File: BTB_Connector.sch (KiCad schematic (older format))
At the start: 1 part

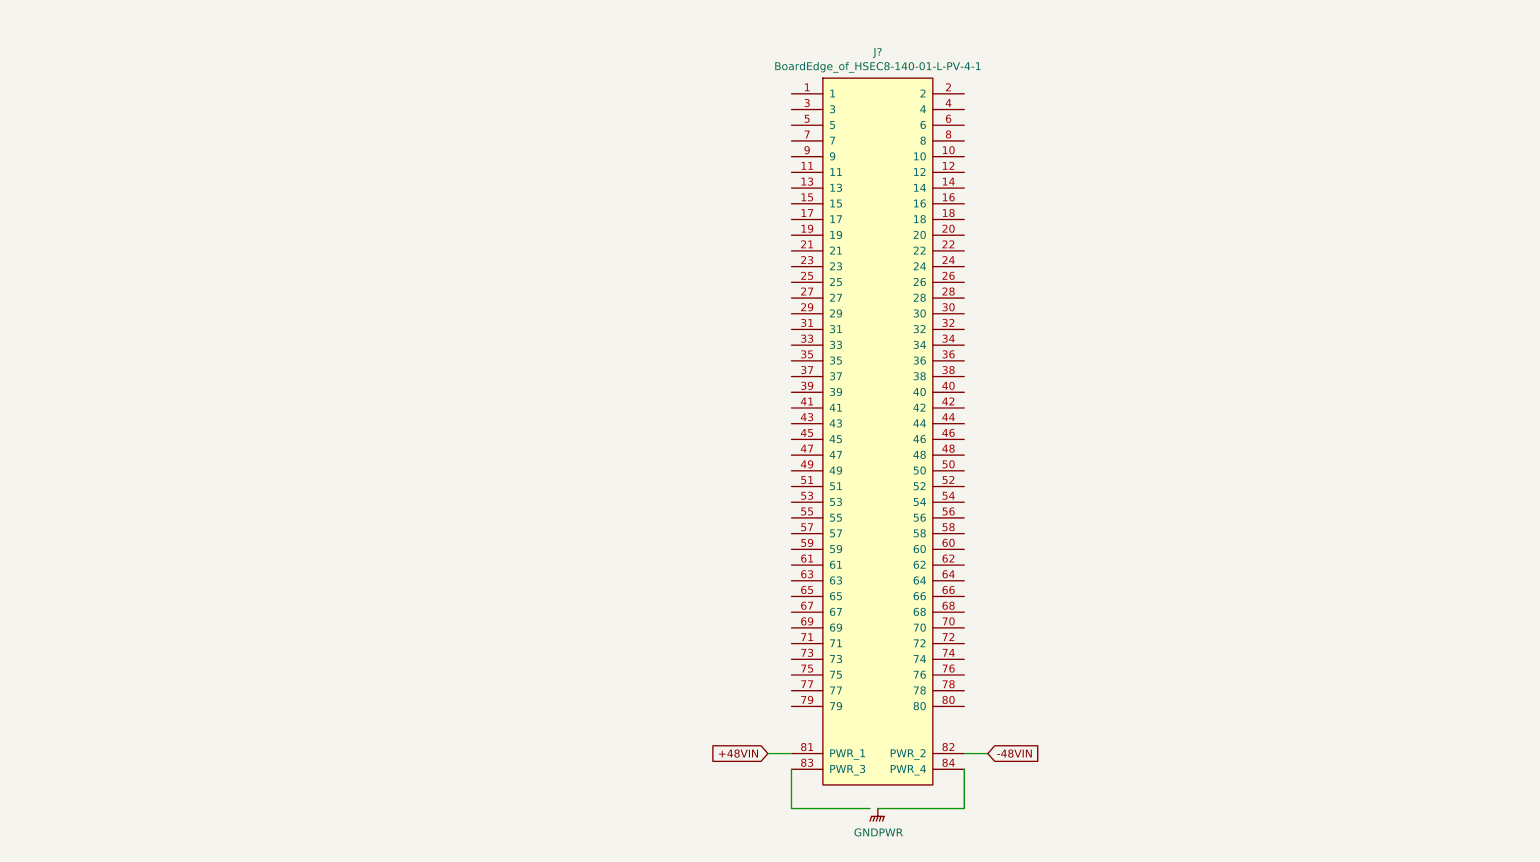
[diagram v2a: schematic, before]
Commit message: -Clock --GND pin was missing. it was added to pin 45 -BTB --pins added
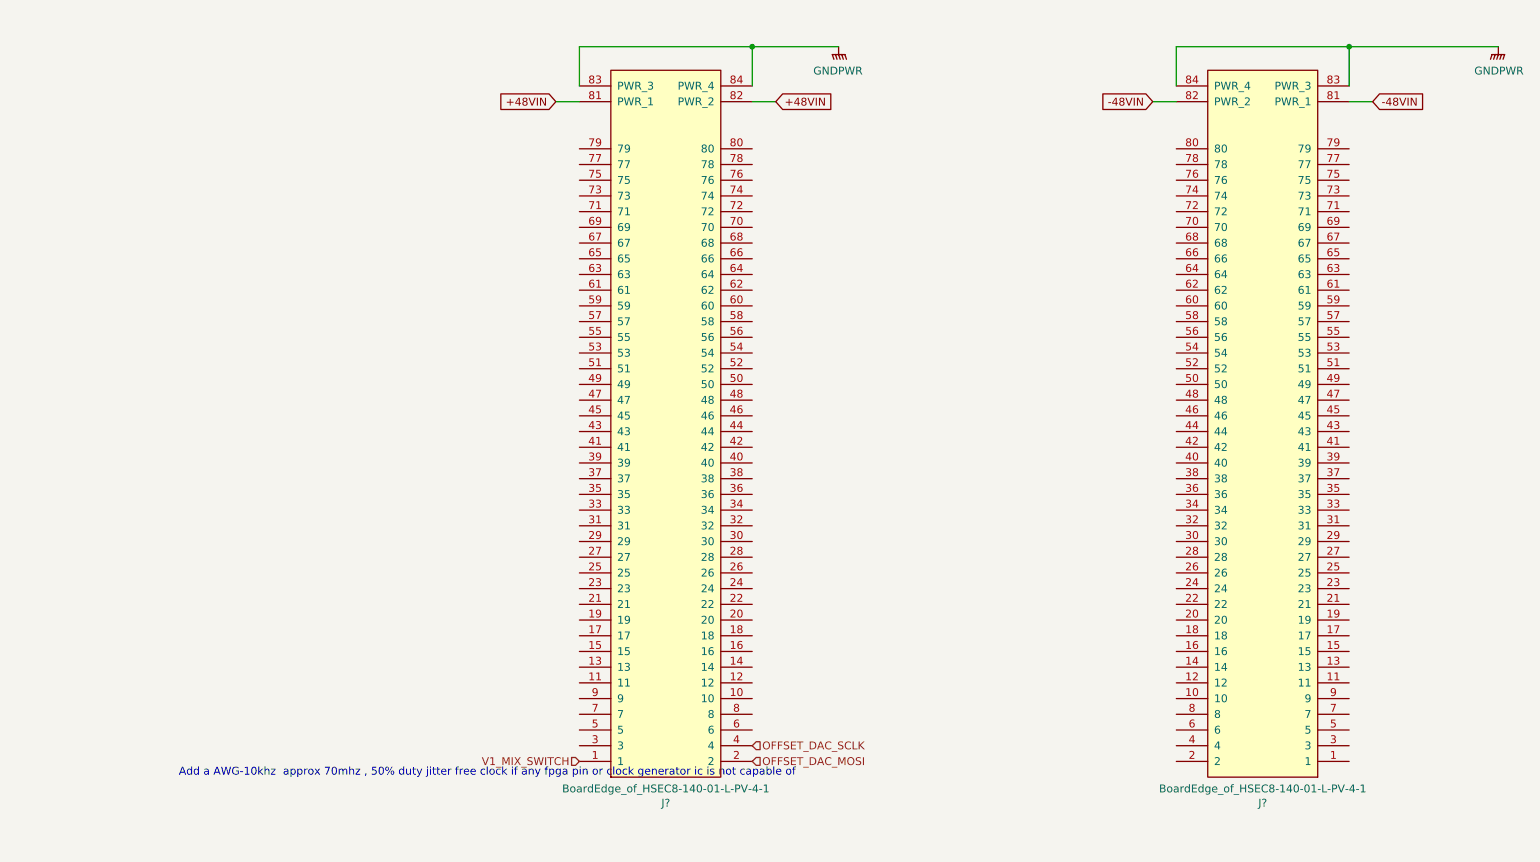
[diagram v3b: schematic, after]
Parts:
- added J?: BoardEdge_of_HSEC8-140-01-L-PV-4-1, GM_Connectors:BoardEdge_of_HSEC8-140-01-L-PV-4-1, symbol GM_Connectors:BoardEdge_of_HSEC8-140-01-L-PV-4-1
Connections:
- net labels added: OFFSET_DAC_MOSI, OFFSET_DAC_SCLK, V1_MIX_SWITCH
- wire segments 6 -> 12
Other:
- note added: "Add a AWG-10khz approx 70mhz , 50% duty jitter free clock if any fpga pin or clock generator ic is not capable of"
- moved on the sheet: J?
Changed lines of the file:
@@
 Comment4 ""
 $EndDescr
+Text GLabel 3400 1650 0    50   Input ~ 0
++48VIN
+Text GLabel 4800 1650 2    50   Input ~ 0
++48VIN
+Wire Wire Line
+	4800 1650 4650 1650
+Wire Wire Line
+	3400 1650 3550 1650
+$Comp
+L power:GNDPWR #PWR?
+U 1 1 602FF0E5
+P 5200 1300
+AR Path="/60256C5F/602FF0E5" Ref="#PWR?"  Part="1"
+AR Path="/601E7B79/602FF0E5" Ref="#PWR?"  Part="1"
+F 0 "#PWR?" H 5200 1100 50  0001 C CNN
+F 1 "GNDPWR" H 5204 1146 50  0000 C CNN
+F 2 "" H 5200 1250 50  0001 C CNN
+F 3 "" H 5200 1250 50  0001 C CNN
+	1    5200 1300
+	-1   0    0    -1
+$EndComp
+Wire Wire Line
+	4650 1550 4650 1300
+Wire Wire Line
+	4650 1300 5200 1300
+Wire Wire Line
+	3550 1300 3550 1550
+$Comp
+L GM_Connectors:BoardEdge_of_HSEC8-140-01-L-PV-4-1 J?
+U 1 1 605943E0
+P 8250 5950
+F 0 "J?" H 8600 6115 50  0000 C CNN
+F 1 "BoardEdge_of_HSEC8-140-01-L-PV-4-1" H 8600 6024 50  0000 C CNN
+F 2 "GM_Connectors:BoardEdge_of_HSEC8-140-01-L-PV-4-1" H 8250 5950 50  0001 C CNN
+F 3 "http://suddendocs.samtec.com/prints/hsec8-1xx-xx-x-pv-x-x-xx-footprint.pdf" H 8250 5950 50  0001 C CNN
+	1    8250 5950
+	-1   0    0    1
+$EndComp
+Text GLabel 8600 1650 2    50   Input ~ 0
+-48VIN
+Text GLabel 7200 1650 0    50   Input ~ 0
+-48VIN
+Wire Wire Line
+	7200 1650 7350 1650
+Wire Wire Line
+	8600 1650 8450 1650
+$Comp
+L power:GNDPWR #PWR?
+U 1 1 6059456A
+P 9400 1300
+AR Path="/60256C5F/6059456A" Ref="#PWR?"  Part="1"
+AR Path="/601E7B79/6059456A" Ref="#PWR?"  Part="1"
+F 0 "#PWR?" H 9400 1100 50  0001 C CNN
+F 1 "GNDPWR" H 9404 1146 50  0000 C CNN
+F 2 "" H 9400 1250 50  0001 C CNN
+F 3 "" H 9400 1250 50  0001 C CNN
+	1    9400 1300
+	1    0    0    -1
+$EndComp
+Wire Wire Line
+	7350 1550 7350 1300
+Wire Wire Line
+	8450 1300 8450 1550
+Wire Wire Line
+	3550 1300 4650 1300
+Connection ~ 4650 1300
+Wire Wire Line
+	9400 1300 8450 1300
+Connection ~ 8450 1300
+Wire Wire Line
+	7350 1300 8450 1300
 $Comp
 L GM_Connectors:BoardEdge_of_HSEC8-140-01-L-PV-4-1 J?
 U 1 1 602EB3A8
-P 5100 1500
-F 0 "J?" H 5450 1665 50  0000 C CNN
-F 1 "BoardEdge_of_HSEC8-140-01-L-PV-4-1" H 5450 1574 50  0000 C CNN
-F 2 "GM_Connectors:BoardEdge_of_HSEC8-140-01-L-PV-4-1" H 5100 1500 50  0001 C CNN
-F 3 "http://suddendocs.samtec.com/prints/hsec8-1xx-xx-x-pv-x-x-xx-footprint.pdf" H 5100 1500 50  0001 C CNN
-	1    5100 1500
-	1    0    0    -1
+P 3750 5950
+F 0 "J?" H 4100 6115 50  0000 C CNN
+F 1 "BoardEdge_of_HSEC8-140-01-L-PV-4-1" H 4100 6024 50  0000 C CNN
+F 2 "GM_Connectors:BoardEdge_of_HSEC8-140-01-L-PV-4-1" H 3750 5950 50  0001 C CNN
+F 3 "http://suddendocs.samtec.com/prints/hsec8-1xx-xx-x-pv-x-x-xx-footprint.pdf" H 3750 5950 50  0001 C CNN
+	1    3750 5950
+	1    0    0    1
 $EndComp
-Text GLabel 4750 5800 0    50   Input ~ 0
-+48VIN
-Text GLabel 6150 5800 2    50   Input ~ 0
--48VIN
-Wire Wire Line
-	6150 5800 6000 5800
-Wire Wire Line
-	4750 5800 4900 5800
-$Comp
-L power:GNDPWR #PWR?
-U 1 1 602FF0E5
-P 5450 6150
-AR Path="/60256C5F/602FF0E5" Ref="#PWR?"  Part="1"
-AR Path="/601E7B79/602FF0E5" Ref="#PWR?"  Part="1"
-F 0 "#PWR?" H 5450 5950 50  0001 C CNN
-F 1 "GNDPWR" H 5454 5996 50  0000 C CNN
-F 2 "" H 5450 6100 50  0001 C CNN
-F 3 "" H 5450 6100 50  0001 C CNN
-	1    5450 6150
-	1    0    0    -1
-$EndComp
-Wire Wire Line
-	6000 5900 6000 6150
-Wire Wire Line
-	6000 6150 5450 6150
-Wire Wire Line
-	5400 6150 4900 6150
-Wire Wire Line
-	4900 6150 4900 5900
+Text HLabel 3550 5850 0    50   Input ~ 0
+V1_MIX_SWITCH
+Text HLabel 4650 5850 2    50   Input ~ 0
+OFFSET_DAC_MOSI
+Text HLabel 4650 5750 2    50   Input ~ 0
+OFFSET_DAC_SCLK
+Text Notes 1000 5950 0    50   ~ 0
+Add a AWG-10khz  approx 70mhz , 50% duty jitter free clock if any fpga pin or clock generator ic is not capable of
 $EndSCHEMATC

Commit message: PCB created and schematics annotated High speed connections added to the BTB
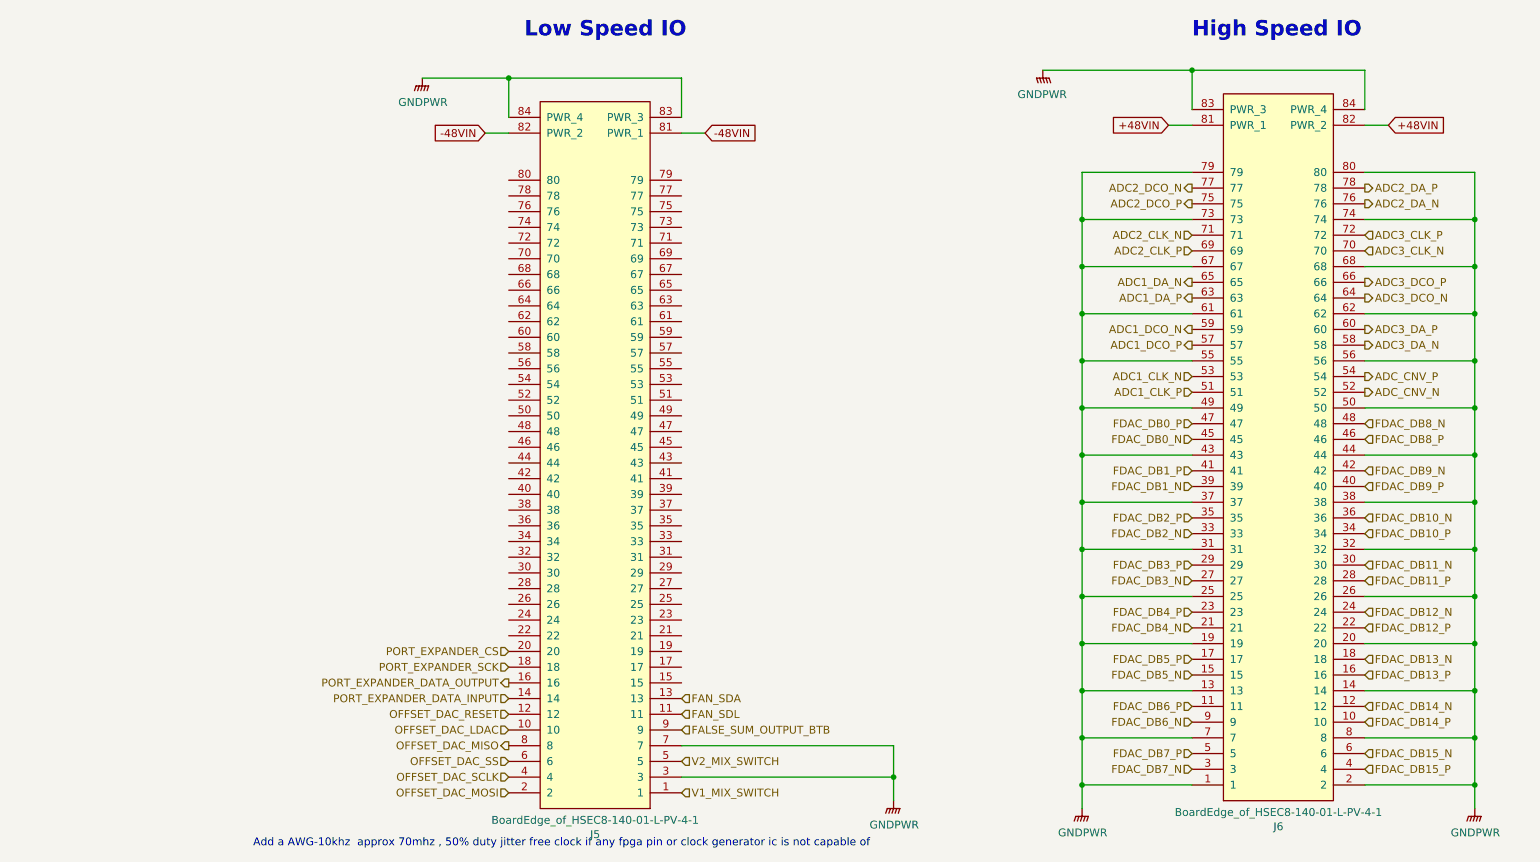
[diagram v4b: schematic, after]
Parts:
- J6: renamed from J?; footprint GM_Connectors:BoardEdge_of_HSEC8-140-01-L-PV-4-1 -> GM_Connectors:HSEC8-140-01-L-PV-4-1
- gave numbers to parts that had none: 1
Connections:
- net +48VIN: now also J6.81 (PWR_1), J6.82 (PWR_2); no longer J5.81 (PWR_1), J5.82 (PWR_2)
- net -48VIN: now also J5.81 (PWR_1), J5.82 (PWR_2); no longer J6.81 (PWR_1), J6.82 (PWR_2)
- net GNDPWR: now also J5.3, J5.7, J6.1, J6.13, J6.14, J6.19, J6.2, J6.20, J6.25, J6.26, J6.31, J6.32, J6.37, J6.38, J6.43, J6.44, J6.49, J6.50, J6.55, J6.56, J6.61, J6.62, J6.67, J6.68, J6.7, J6.73, J6.74, J6.79, J6.8, J6.80
- net OFFSET_DAC_LDAC: now reaches J5.10
- net FAN_SDL: now reaches J5.11
- net OFFSET_DAC_RESET: now reaches J5.12
- net FAN_SDA: now reaches J5.13
- net PORT_EXPANDER_DATA_INPUT: now reaches J5.14
- net PORT_EXPANDER_DATA_OUTPUT: now reaches J5.16
- net PORT_EXPANDER_SCK: now reaches J5.18
- net PORT_EXPANDER_CS: now reaches J5.20
- net V2_MIX_SWITCH: now reaches J5.5
- net OFFSET_DAC_SS: now reaches J5.6
- net OFFSET_DAC_MISO: now reaches J5.8
- net FALSE_SUM_OUTPUT_BTB: now reaches J5.9
- net FDAC_DB14_P: now reaches J6.10
- net FDAC_DB6_P: now reaches J6.11
- net FDAC_DB14_N: now reaches J6.12
- net FDAC_DB5_N: now reaches J6.15
- net FDAC_DB13_P: now reaches J6.16
- net FDAC_DB5_P: now reaches J6.17
- net FDAC_DB13_N: now reaches J6.18
- net FDAC_DB4_N: now reaches J6.21
- net FDAC_DB12_P: now reaches J6.22
- net FDAC_DB4_P: now reaches J6.23
- net FDAC_DB12_N: now reaches J6.24
- net FDAC_DB3_N: now reaches J6.27
- net FDAC_DB11_P: now reaches J6.28
- net FDAC_DB3_P: now reaches J6.29
- net FDAC_DB7_N: now reaches J6.3
- net FDAC_DB11_N: now reaches J6.30
- net FDAC_DB2_N: now reaches J6.33
- net FDAC_DB10_P: now reaches J6.34
- net FDAC_DB2_P: now reaches J6.35
- net FDAC_DB10_N: now reaches J6.36
- net FDAC_DB1_N: now reaches J6.39
- net FDAC_DB15_P: now reaches J6.4
- net FDAC_DB9_P: now reaches J6.40
- net FDAC_DB1_P: now reaches J6.41
- net FDAC_DB9_N: now reaches J6.42
- net FDAC_DB0_N: now reaches J6.45
- net FDAC_DB8_P: now reaches J6.46
- net FDAC_DB0_P: now reaches J6.47
- net FDAC_DB8_N: now reaches J6.48
- net FDAC_DB7_P: now reaches J6.5
- net ADC1_CLK_P: now reaches J6.51
- net ADC_CNV_N: now reaches J6.52
- net ADC1_CLK_N: now reaches J6.53
- net ADC_CNV_P: now reaches J6.54
- net ADC1_DCO_P: now reaches J6.57
- net ADC3_DA_N: now reaches J6.58
- net ADC1_DCO_N: now reaches J6.59
- net FDAC_DB15_N: now reaches J6.6
- net ADC3_DA_P: now reaches J6.60
- net ADC1_DA_P: now reaches J6.63
- net ADC3_DCO_N: now reaches J6.64
- net ADC1_DA_N: now reaches J6.65
- net ADC3_DCO_P: now reaches J6.66
- net ADC2_CLK_P: now reaches J6.69
- net ADC3_CLK_N: now reaches J6.70
- net ADC2_CLK_N: now reaches J6.71
- net ADC3_CLK_P: now reaches J6.72
- net ADC2_DCO_P: now reaches J6.75
- net ADC2_DA_N: now reaches J6.76
- net ADC2_DCO_N: now reaches J6.77
- net ADC2_DA_P: now reaches J6.78
- net FDAC_DB6_N: now reaches J6.9
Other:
- note added: "High Speed IO"
- note added: "Low Speed IO"
- moved on the sheet: J5, J6

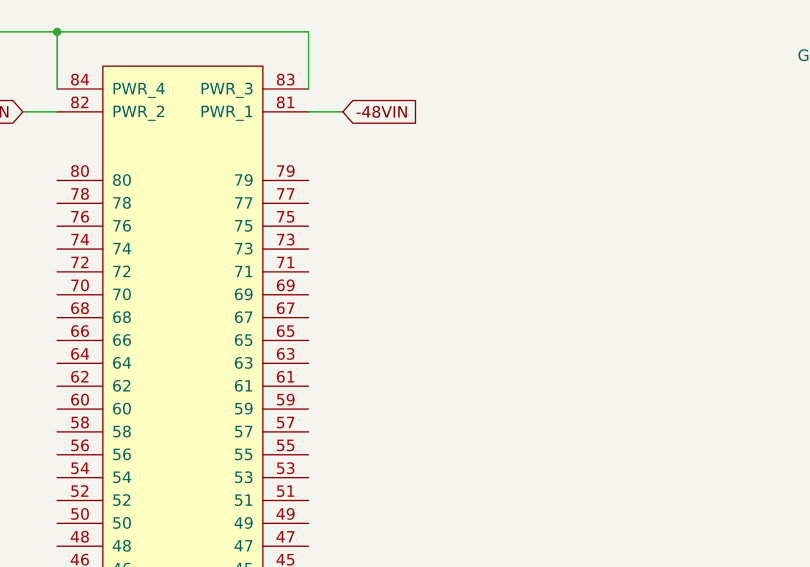
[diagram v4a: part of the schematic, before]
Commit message: BTB and FPGA pins added and connections were made
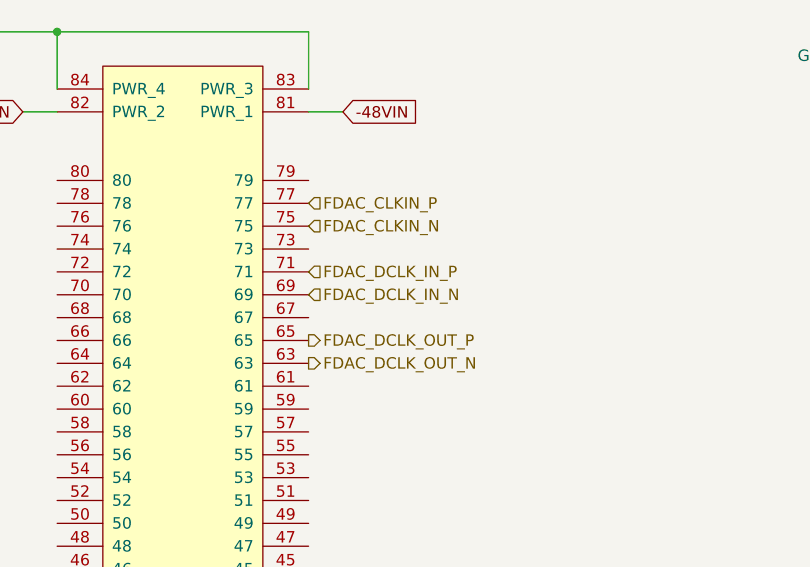
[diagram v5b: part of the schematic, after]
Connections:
- net FDAC_DCLK_OUT_N: now reaches J5.63
- net FDAC_DCLK_OUT_P: now reaches J5.65
- net FDAC_DCLK_IN_N: now reaches J5.69
- net FDAC_DCLK_IN_P: now reaches J5.71
- net FDAC_CLKIN_N: now reaches J5.75
- net FDAC_CLKIN_P: now reaches J5.77
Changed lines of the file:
@@
 Wire Wire Line
 	6750 2400 6750 2700
+Text HLabel 4200 2650 2    50   Input ~ 0
+FDAC_DCLK_IN_N
+Text HLabel 4200 2250 2    50   Input ~ 0
+FDAC_CLKIN_P
+Text HLabel 4200 2350 2    50   Input ~ 0
+FDAC_CLKIN_N
+Text HLabel 4200 2850 2    50   Output ~ 0
+FDAC_DCLK_OUT_P
+Text HLabel 4200 2950 2    50   Output ~ 0
+FDAC_DCLK_OUT_N
+Text HLabel 4200 2550 2    50   Input ~ 0
+FDAC_DCLK_IN_P
 $EndSCHEMATC

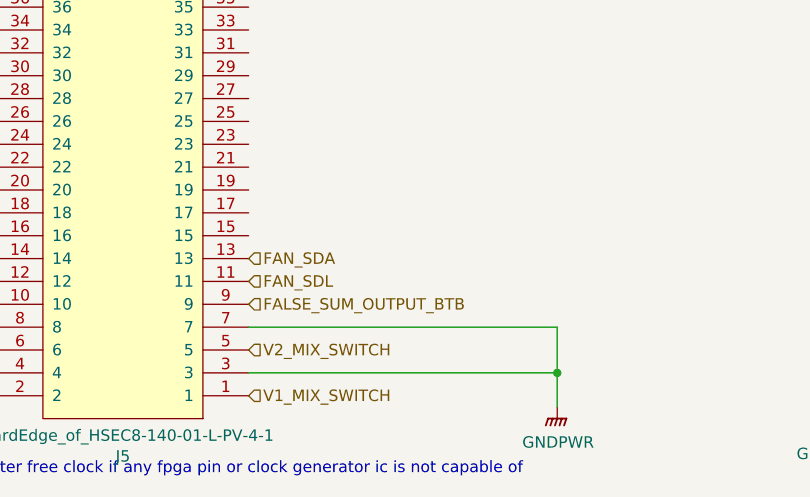
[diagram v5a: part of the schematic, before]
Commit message: Connections were made to FPGA banks
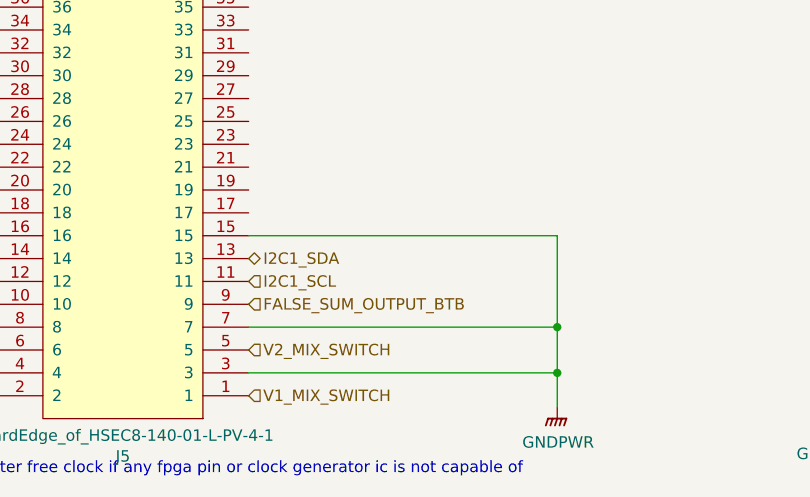
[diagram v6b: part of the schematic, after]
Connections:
- net GNDPWR: now also J5.15
- net FAN_SDA renamed I2C1_SDA
- net FAN_SDL renamed I2C1_SCL
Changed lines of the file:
@@
 Text HLabel 3100 5650 0    50   Input ~ 0
 OFFSET_DAC_LDAC
-Text HLabel 4200 5550 2    50   Input ~ 0
-FAN_SDL
 Text HLabel 3100 5550 0    50   Input ~ 0
 OFFSET_DAC_RESET
-Text HLabel 4200 5450 2    50   Input ~ 0
-FAN_SDA
 Text HLabel 3100 5450 0    50   Input ~ 0
 PORT_EXPANDER_DATA_INPUT
@@
 Text HLabel 4200 2550 2    50   Input ~ 0
 FDAC_DCLK_IN_P
+Text HLabel 4200 5450 2    50   BiDi ~ 0
+I2C1_SDA
+Text HLabel 4200 5550 2    50   Input ~ 0
+I2C1_SCL
+Wire Wire Line
+	4200 5350 5550 5350
+Wire Wire Line
+	5550 5350 5550 5750
+Connection ~ 5550 5750
 $EndSCHEMATC
